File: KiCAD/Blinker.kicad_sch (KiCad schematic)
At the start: 0 parts

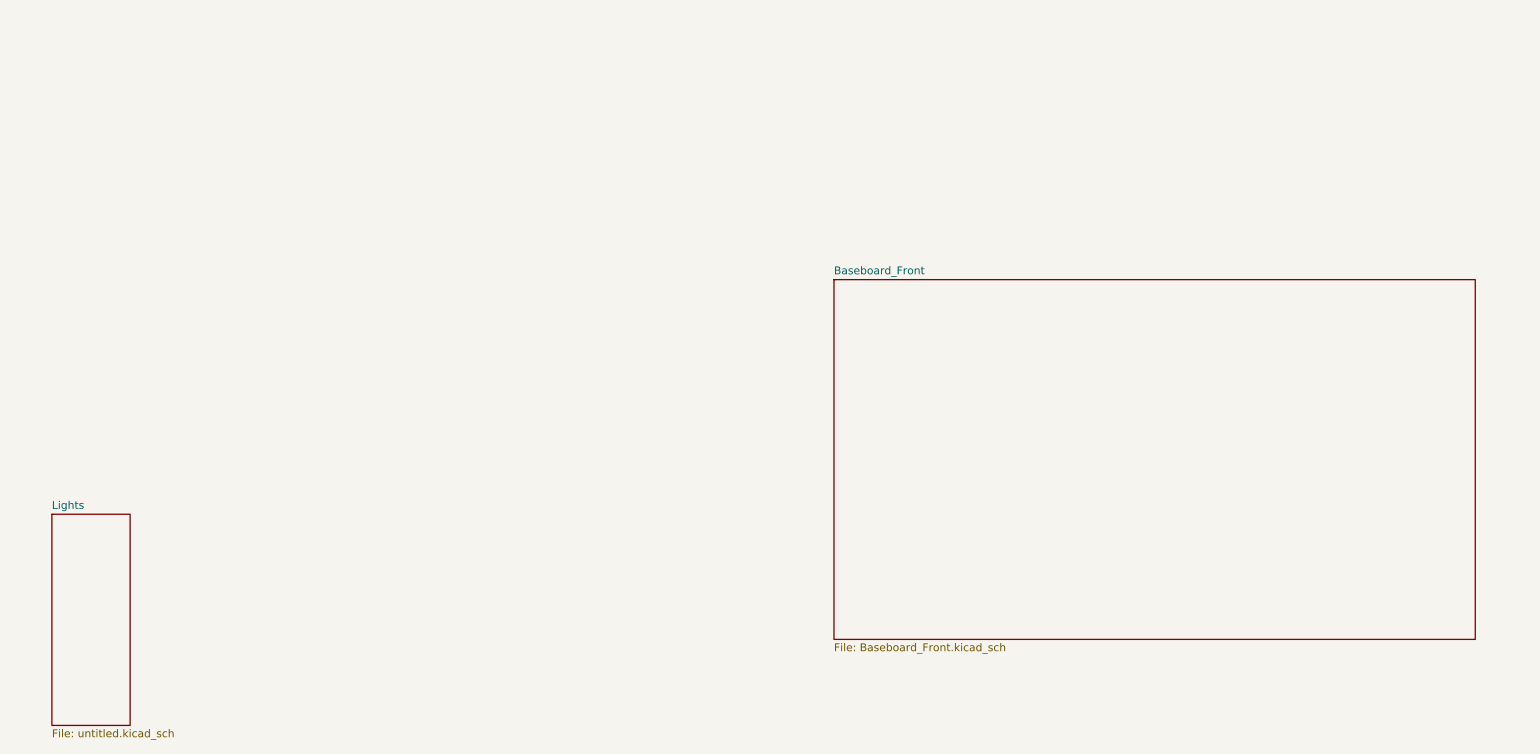
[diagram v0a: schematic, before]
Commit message: updated structure, new components
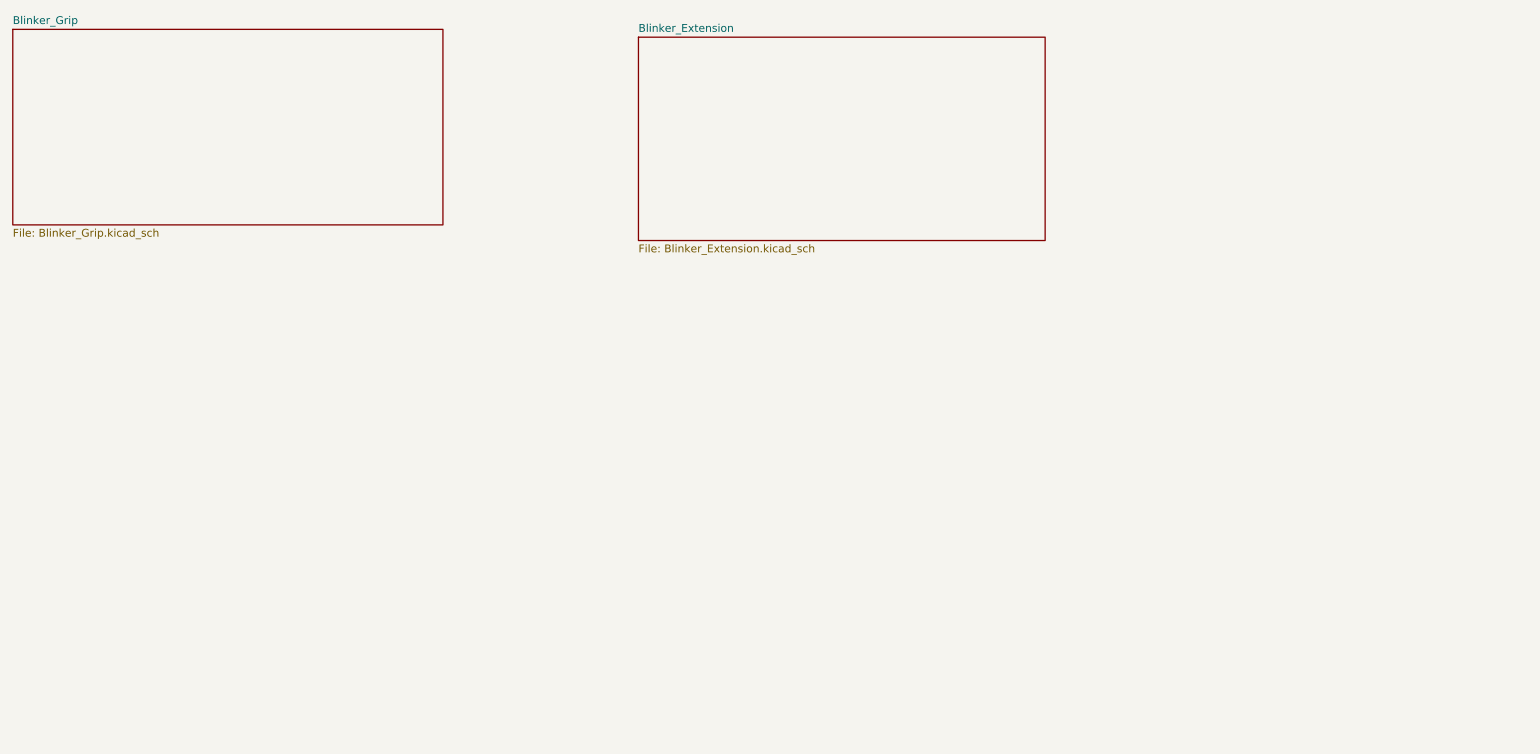
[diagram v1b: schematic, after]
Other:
- removed sheet Baseboard_Front
- removed sheet Lights
- added sheet Blinker_Extension (Blinker_Extension.kicad_sch)
- added sheet Blinker_Grip (Blinker_Grip.kicad_sch)
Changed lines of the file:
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@@
 	(generator "eeschema")
 	(generator_version "9.0")
-	(paper "A3")
+	(paper "A4")
 	(sheet
-		(at 147.32 88.9)
-		(size 104.14 58.42)
+		(at 13.97 48.26)
+		(size 69.85 31.75)
 		(exclude_from_sim no)
 		(in_bom yes)
@@
 			(color 0 0 0 0.0000)
 		)
-		(property "Sheetname" "Baseboard_Front"
-			(at 147.32 88.1884 0)
+		(property "Sheetname" "Blinker_Grip"
+			(at 13.97 47.5484 0)
 			(effects
 				(font
@@
 			)
 		)
-		(property "Sheetfile" "Baseboard_Front.kicad_sch"
-			(at 147.32 147.9046 0)
+		(property "Sheetfile" "Blinker_Grip.kicad_sch"
+			(at 13.97 80.5946 0)
 			(effects
 				(font
@@
 		(instances
 			(project "PedalPirat"
-				(path "/9ce0a74b-6fd5-414b-86b4-a0501b0597ae"
-					(page "7")
+				(path "/9ce0a74b-6fd5-414b-86b4-a0501b0597ae/cea94e63-79b8-4dd4-b152-d849d09f7588/8683f94c-03a2-4fd0-82d4-d6d06d12115e"
+					(page "4")
 				)
 			)
@@
 	)
 	(sheet
-		(at 20.32 127)
-		(size 12.7 34.29)
+		(at 115.57 49.53)
+		(size 66.04 33.02)
 		(exclude_from_sim no)
 		(in_bom yes)
@@
 			(color 0 0 0 0.0000)
 		)
-		(property "Sheetname" "Lights"
-			(at 20.32 126.2884 0)
+		(property "Sheetname" "Blinker_Extension"
+			(at 115.57 48.8184 0)
 			(effects
 				(font
@@
 			)
 		)
-		(property "Sheetfile" "untitled.kicad_sch"
-			(at 20.32 161.8746 0)
+		(property "Sheetfile" "Blinker_Extension.kicad_sch"
+			(at 115.57 83.1346 0)
 			(effects
 				(font
@@
 		(instances
 			(project "PedalPirat"
-				(path "/9ce0a74b-6fd5-414b-86b4-a0501b0597ae"
-					(page "2")
+				(path "/9ce0a74b-6fd5-414b-86b4-a0501b0597ae/cea94e63-79b8-4dd4-b152-d849d09f7588/8683f94c-03a2-4fd0-82d4-d6d06d12115e"
+					(page "5")
 				)
 			)
 		)
 	)
-	(sheet_instances
-		(path "/"
-			(page "1")
-		)
-	)
-	(embedded_fonts no)
 )

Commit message: updated shit
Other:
- added sheet Blinker_Handlebarextension (Blinker_Handlebarextension.kicad_sch)
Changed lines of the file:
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@@
 	(paper "A4")
+	(sheet
+		(at 209.55 91.44)
+		(size 45.72 24.13)
+		(exclude_from_sim no)
+		(in_bom yes)
+		(on_board yes)
+		(dnp no)
+		(fields_autoplaced yes)
+		(stroke
+			(width 0.1524)
+			(type solid)
+		)
+		(fill
+			(color 0 0 0 0.0000)
+		)
+		(property "Sheetname" "Blinker_Handlebarextension"
+			(at 209.55 90.7284 0)
+			(effects
+				(font
+					(size 1.27 1.27)
+				)
+				(justify left bottom)
+			)
+		)
+		(property "Sheetfile" "Blinker_Handlebarextension.kicad_sch"
+			(at 209.55 116.1546 0)
+			(effects
+				(font
+					(size 1.27 1.27)
+				)
+				(justify left top)
+			)
+		)
+		(instances
+			(project "PedalPirat"
+				(path "/9ce0a74b-6fd5-414b-86b4-a0501b0597ae/cea94e63-79b8-4dd4-b152-d849d09f7588/8683f94c-03a2-4fd0-82d4-d6d06d12115e"
+					(page "9")
+				)
+			)
+		)
+	)
 	(sheet
 		(at 13.97 48.26)
